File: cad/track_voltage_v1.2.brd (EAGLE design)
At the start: 38.5 x 32.5 mm, 37 parts, among them U2 74HC4051D, X1 1751248

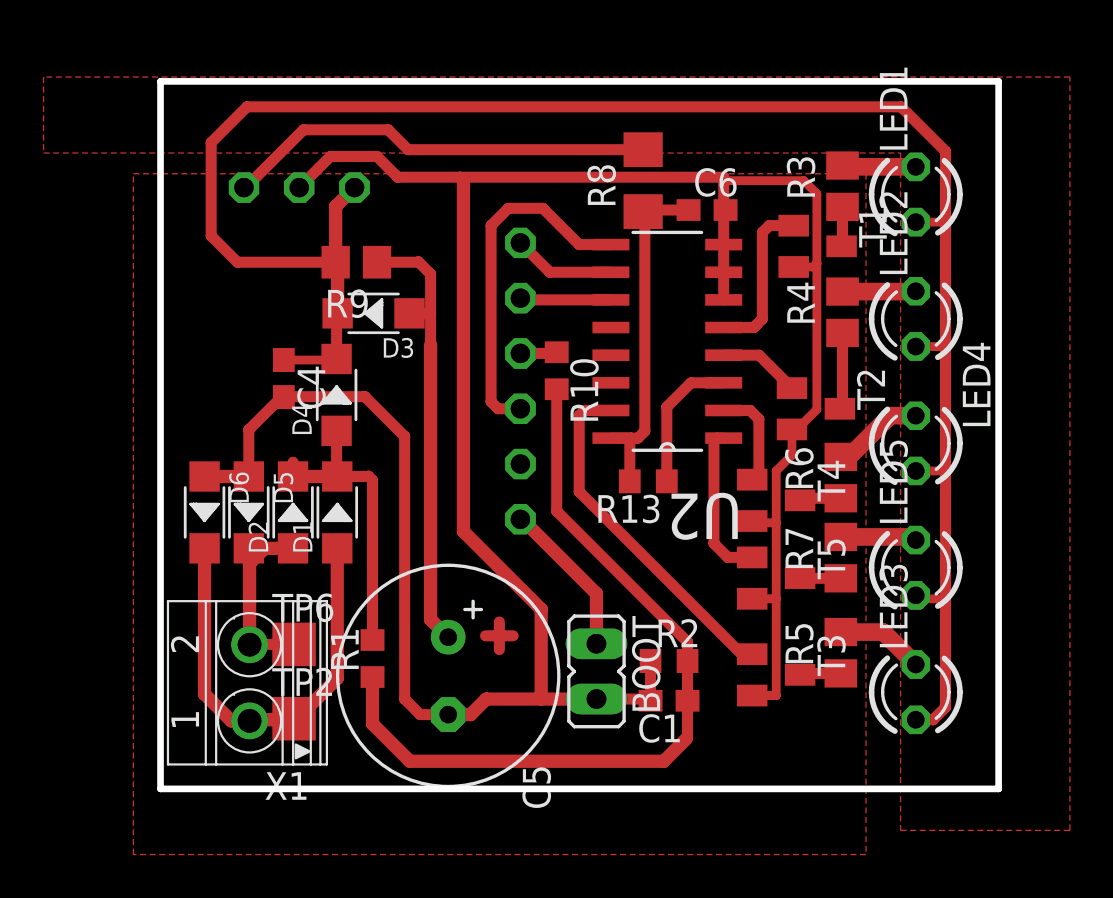
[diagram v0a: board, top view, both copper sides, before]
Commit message: Added some docs, updated code. Updated schematic to use PB5.
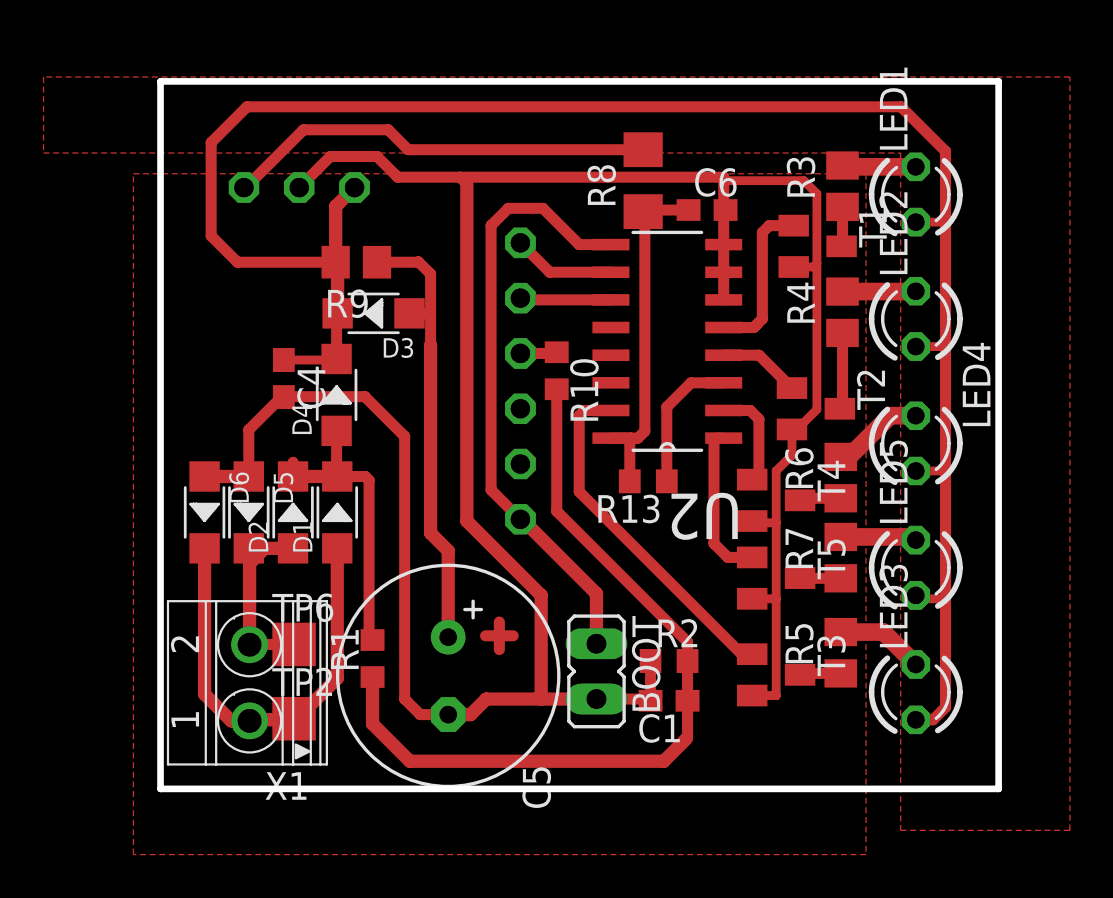
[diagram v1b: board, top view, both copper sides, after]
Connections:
- removed net N$1: BOOT.1, U$2.P5
- net S2: now also BOOT.1, U$2.P5; no longer U$2.P3
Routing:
- net S2: track 16.1 -> 27.8 mm
- net N$1: track 7.21 -> 0.00 mm
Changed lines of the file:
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@@
 <wire x1="14.462375" y1="4.1275" x2="13.748125" y2="3.41325" width="0.6096" layer="1"/>
 <wire x1="13.748125" y1="3.41325" x2="12.71625" y2="3.41325" width="0.6096" layer="1"/>
-<wire x1="16.98625" y1="4.1275" x2="16.98625" y2="8.255" width="0.6096" layer="1"/>
-<wire x1="16.98625" y1="8.255" x2="13.414375" y2="11.826875" width="0.6096" layer="1"/>
-<wire x1="13.414375" y1="11.826875" x2="13.414375" y2="27.94" width="0.6096" layer="1"/>
+<wire x1="16.98625" y1="4.1275" x2="16.98625" y2="8.89" width="0.6096" layer="1"/>
+<wire x1="16.98625" y1="8.89" x2="13.573125" y2="12.303125" width="0.6096" layer="1"/>
+<wire x1="13.573125" y1="12.303125" x2="13.573125" y2="27.78125" width="0.6096" layer="1"/>
 <wire x1="25.371425" y1="28.09875" x2="13.255625" y2="28.09875" width="0.508" layer="1"/>
 <wire x1="13.255625" y1="28.09875" x2="10.398125" y2="28.09875" width="0.508" layer="1"/>
@@
 <wire x1="5.87375" y1="27.6225" x2="7.3025" y2="29.05125" width="0.508" layer="1"/>
 <wire x1="9.445625" y1="29.05125" x2="10.398125" y2="28.09875" width="0.508" layer="1"/>
-<wire x1="13.255625" y1="28.09875" x2="13.414375" y2="27.94" width="0.508" layer="1"/>
+<wire x1="13.255625" y1="28.09875" x2="13.573125" y2="27.78125" width="0.508" layer="1"/>
 <wire x1="7.3025" y1="29.05125" x2="9.445625" y2="29.05125" width="0.508" layer="1"/>
 <wire x1="12.71625" y1="3.41325" x2="11.429875" y2="3.41325" width="0.508" layer="1"/>
@@
 <contactref element="R9" pad="1"/>
 <contactref element="D3" pad="+"/>
-<wire x1="12.71625" y1="6.96925" x2="11.90625" y2="7.77925" width="0.6096" layer="1"/>
-<wire x1="11.90625" y1="7.77925" x2="11.90625" y2="20.399375" width="0.6096" layer="1"/>
+<wire x1="12.71625" y1="6.96925" x2="12.71625" y2="10.938" width="0.6096" layer="1"/>
+<wire x1="12.71625" y1="10.938" x2="11.90625" y2="11.748" width="0.6096" layer="1"/>
+<wire x1="11.90625" y1="11.748" x2="11.90625" y2="20.399375" width="0.6096" layer="1"/>
 <wire x1="11.90625" y1="20.399375" x2="11.90625" y2="21.828125" width="0.508" layer="1"/>
 <wire x1="11.90625" y1="21.828125" x2="11.90625" y2="23.65375" width="0.508" layer="1"/>
@@
 <wire x1="7.58825" y1="16.4465" x2="7.58825" y2="14.38275" width="0.508" layer="1"/>
 <wire x1="7.62" y1="14.351" x2="7.58825" y2="14.38275" width="0.508" layer="1"/>
-<wire x1="9.239375" y1="6.838125" x2="9.239375" y2="14.17625" width="0.508" layer="1"/>
-<wire x1="9.239375" y1="14.17625" x2="9.04875" y2="14.366875" width="0.508" layer="1"/>
-<wire x1="9.04875" y1="14.366875" x2="9.032875" y2="14.351" width="0.508" layer="1"/>
-<wire x1="9.032875" y1="14.351" x2="7.62" y2="14.351" width="0.508" layer="1"/>
+<wire x1="9.080625" y1="14.17625" x2="9.080625" y2="6.996875" width="0.508" layer="1"/>
+<wire x1="9.239375" y1="6.838125" x2="9.080625" y2="6.996875" width="0.508" layer="1"/>
+<wire x1="9.080625" y1="14.17625" x2="8.905875" y2="14.351" width="0.508" layer="1"/>
+<wire x1="8.905875" y1="14.351" x2="7.62" y2="14.351" width="0.508" layer="1"/>
 </signal>
 <signal name="N$26">
@@
 <wire x1="28.89145" y1="9.67355" x2="28.88125" y2="9.68375" width="0.508" layer="1"/>
 </signal>
-<signal name="N$1">
+<signal name="N$2">
+<contactref element="U$2" pad="P2"/>
+<contactref element="R10" pad="1"/>
+<wire x1="16.03375" y1="20.0025" x2="17.644375" y2="20.0025" width="0.508" layer="1"/>
+<wire x1="17.644375" y1="20.0025" x2="17.700625" y2="20.05875" width="0.508" layer="1"/>
+</signal>
+<signal name="S0">
+<contactref element="U2" pad="11"/>
+<contactref element="U$2" pad="P1"/>
+<wire x1="20.189825" y1="22.463125" x2="16.113125" y2="22.463125" width="0.508" layer="1"/>
+<wire x1="16.113125" y1="22.463125" x2="16.03375" y2="22.5425" width="0.508" layer="1"/>
+</signal>
+<signal name="S1">
+<contactref element="U2" pad="10"/>
+<contactref element="U$2" pad="P0"/>
+<wire x1="20.189825" y1="23.733125" x2="17.383125" y2="23.733125" width="0.508" layer="1"/>
+<wire x1="17.383125" y1="23.733125" x2="16.03375" y2="25.0825" width="0.508" layer="1"/>
+</signal>
+<signal name="S2">
+<contactref element="U2" pad="9"/>
+<wire x1="20.189825" y1="25.003125" x2="18.7325" y2="25.003125" width="0.508" layer="1"/>
+<wire x1="18.7325" y1="25.003125" x2="17.065625" y2="26.67" width="0.508" layer="1"/>
+<wire x1="17.065625" y1="26.67" x2="15.478125" y2="26.67" width="0.508" layer="1"/>
+<wire x1="14.684375" y1="25.87625" x2="14.684375" y2="13.731875" width="0.508" layer="1"/>
+<wire x1="15.478125" y1="26.67" x2="14.684375" y2="25.87625" width="0.508" layer="1"/>
 <contactref element="BOOT" pad="1"/>
 <contactref element="U$2" pad="P5"/>
@@
 <wire x1="16.03375" y1="12.3825" x2="16.113125" y2="12.3825" width="0.6096" layer="1"/>
 <wire x1="19.52625" y1="6.6675" x2="19.52625" y2="8.969375" width="0.6096" layer="1"/>
-</signal>
-<signal name="N$2">
-<contactref element="U$2" pad="P2"/>
-<contactref element="R10" pad="1"/>
-<wire x1="16.03375" y1="20.0025" x2="17.644375" y2="20.0025" width="0.508" layer="1"/>
-<wire x1="17.644375" y1="20.0025" x2="17.700625" y2="20.05875" width="0.508" layer="1"/>
-</signal>
-<signal name="S0">
-<contactref element="U2" pad="11"/>
-<contactref element="U$2" pad="P1"/>
-<wire x1="20.189825" y1="22.463125" x2="16.113125" y2="22.463125" width="0.508" layer="1"/>
-<wire x1="16.113125" y1="22.463125" x2="16.03375" y2="22.5425" width="0.508" layer="1"/>
-</signal>
-<signal name="S1">
-<contactref element="U2" pad="10"/>
-<contactref element="U$2" pad="P0"/>
-<wire x1="20.189825" y1="23.733125" x2="17.383125" y2="23.733125" width="0.508" layer="1"/>
-<wire x1="17.383125" y1="23.733125" x2="16.03375" y2="25.0825" width="0.508" layer="1"/>
-</signal>
-<signal name="S2">
-<contactref element="U2" pad="9"/>
-<contactref element="U$2" pad="P3"/>
-<wire x1="20.189825" y1="25.003125" x2="18.7325" y2="25.003125" width="0.508" layer="1"/>
-<wire x1="18.7325" y1="25.003125" x2="17.065625" y2="26.67" width="0.508" layer="1"/>
-<wire x1="17.065625" y1="26.67" x2="15.478125" y2="26.67" width="0.508" layer="1"/>
-<wire x1="14.684375" y1="25.87625" x2="14.684375" y2="17.78" width="0.508" layer="1"/>
-<wire x1="14.684375" y1="17.78" x2="15.001875" y2="17.4625" width="0.508" layer="1"/>
-<wire x1="15.001875" y1="17.4625" x2="16.03375" y2="17.4625" width="0.508" layer="1"/>
-<wire x1="15.478125" y1="26.67" x2="14.684375" y2="25.87625" width="0.508" layer="1"/>
+<wire x1="16.03375" y1="12.3825" x2="14.684375" y2="13.731875" width="0.508" layer="1"/>
 </signal>
 <signal name="N$3">
